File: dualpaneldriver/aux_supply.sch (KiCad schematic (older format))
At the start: 42 parts, among them J201 Conn_01x04, J202 Conn_01x04, Q201 BSS123, Q202 DMP10H400SK3-13, U201 INA190A2-Q1, U202 SY8502, U203 MCP1754ST-3302E/MB

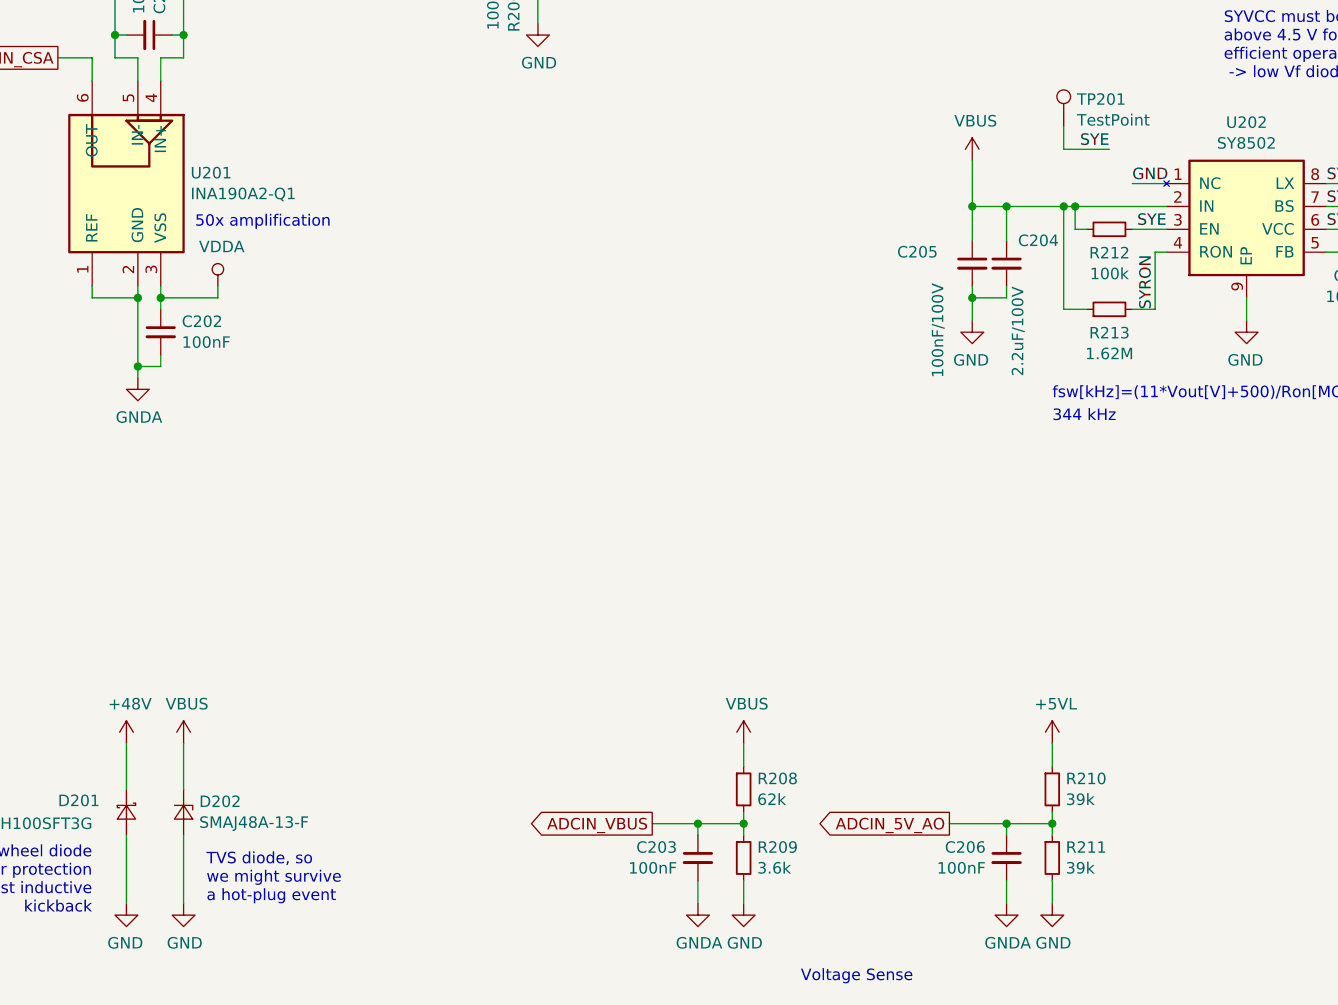
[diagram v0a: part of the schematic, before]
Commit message: some components placed
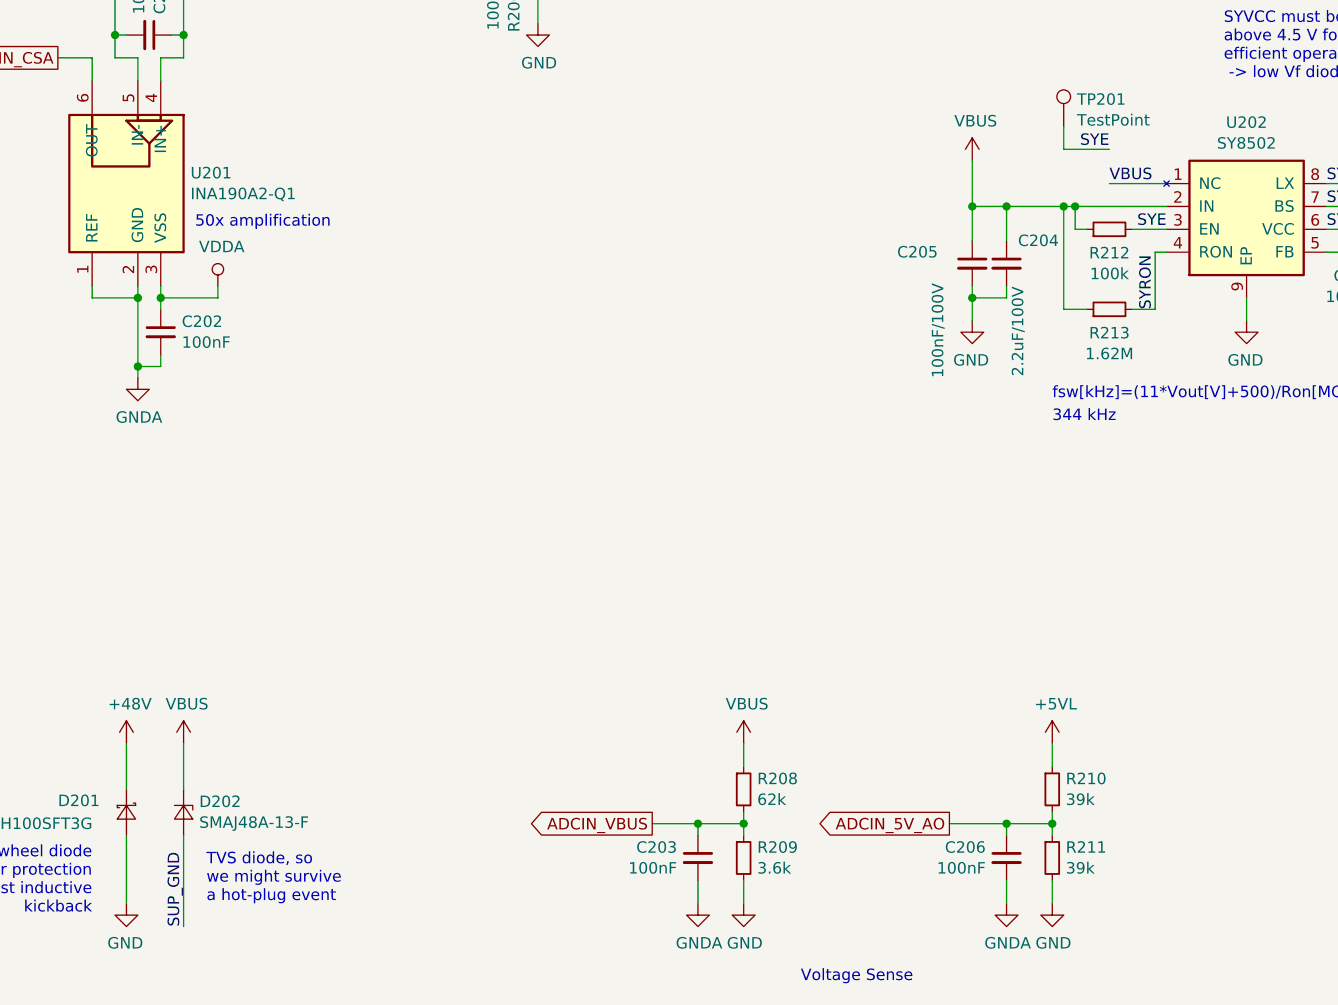
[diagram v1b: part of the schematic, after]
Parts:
- TP201: footprint (none) -> TestPoint:TestPoint_Pad_1.0x1.0mm
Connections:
- net GND: no longer D202.2 (A), U202.1 (NC)
- net SUP_GND: now also D202.2 (A)
- net VBUS: now also U202.1 (NC)
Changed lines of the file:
@@
 	-1   0    0    -1
 $EndComp
-$Comp
-L power:GND #PWR?
-U 1 1 5E2BDC3A
-P 2450 7250
-AR Path="/5DC18D84/5E17ED97/5E2BDC3A" Ref="#PWR?"  Part="1"
-AR Path="/5DC18D84/5E2BDC3A" Ref="#PWR0206"  Part="1"
-F 0 "#PWR0206" H 2450 7000 50  0001 C CNN
-F 1 "GND" H 2455 7077 50  0000 C CNN
-F 2 "" H 2450 7250 50  0001 C CNN
-F 3 "" H 2450 7250 50  0001 C CNN
-	1    2450 7250
-	1    0    0    -1
-$EndComp
-Wire Wire Line
-	2450 7250 2450 6950
+Wire Wire Line
+	2450 7350 2450 6950
 Wire Wire Line
 	2450 6750 2450 6550
@@
 F 0 "TP201" H 6358 3968 50  0000 L CNN
 F 1 "TestPoint" H 6358 3877 50  0000 L CNN
-F 2 "" H 6500 3850 50  0001 C CNN
+F 2 "TestPoint:TestPoint_Pad_1.0x1.0mm" H 6500 3850 50  0001 C CNN
 F 3 "~" H 6500 3850 50  0001 C CNN
 	1    6300 3850
@@
 $EndComp
 Wire Wire Line
-	6750 4100 6600 4100
-Text Label 6600 4100 0    50   ~ 0
-GND
+	6750 4100 6500 4100
+Text Label 6500 4100 0    50   ~ 0
+VBUS
 $Comp
 L Device:L_Core_Ferrite_Small L?
@@
 Wire Wire Line
 	5100 1800 5100 2000
+Text Label 2450 7350 1    50   ~ 0
+SUP_GND
 $EndSCHEMATC

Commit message: changed input cap on the LED driver's DCDC
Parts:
- C205: footprint Capacitor_SMD:C_0603_1608Metric -> Capacitor_SMD:C_1210_3225Metric
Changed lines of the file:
@@
 F 0 "C205" H 5750 4500 50  0000 R CNN
 F 1 "2.2uF/100V" V 6100 4350 50  0000 R CNN
-F 2 "Capacitor_SMD:C_0603_1608Metric" H 6050 4450 50  0001 C CNN
+F 2 "Capacitor_SMD:C_1210_3225Metric" H 6050 4450 50  0001 C CNN
 F 3 "~" H 6050 4450 50  0001 C CNN
 	1    6050 4450
